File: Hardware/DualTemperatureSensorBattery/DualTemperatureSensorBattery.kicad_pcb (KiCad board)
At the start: 2 copper layers, 67.5 x 24.2 mm, 22 parts, among them J2 Conn_01x06, Q101 BSS84, SW2 SW_Push, U1 ME54BS01_V1.0

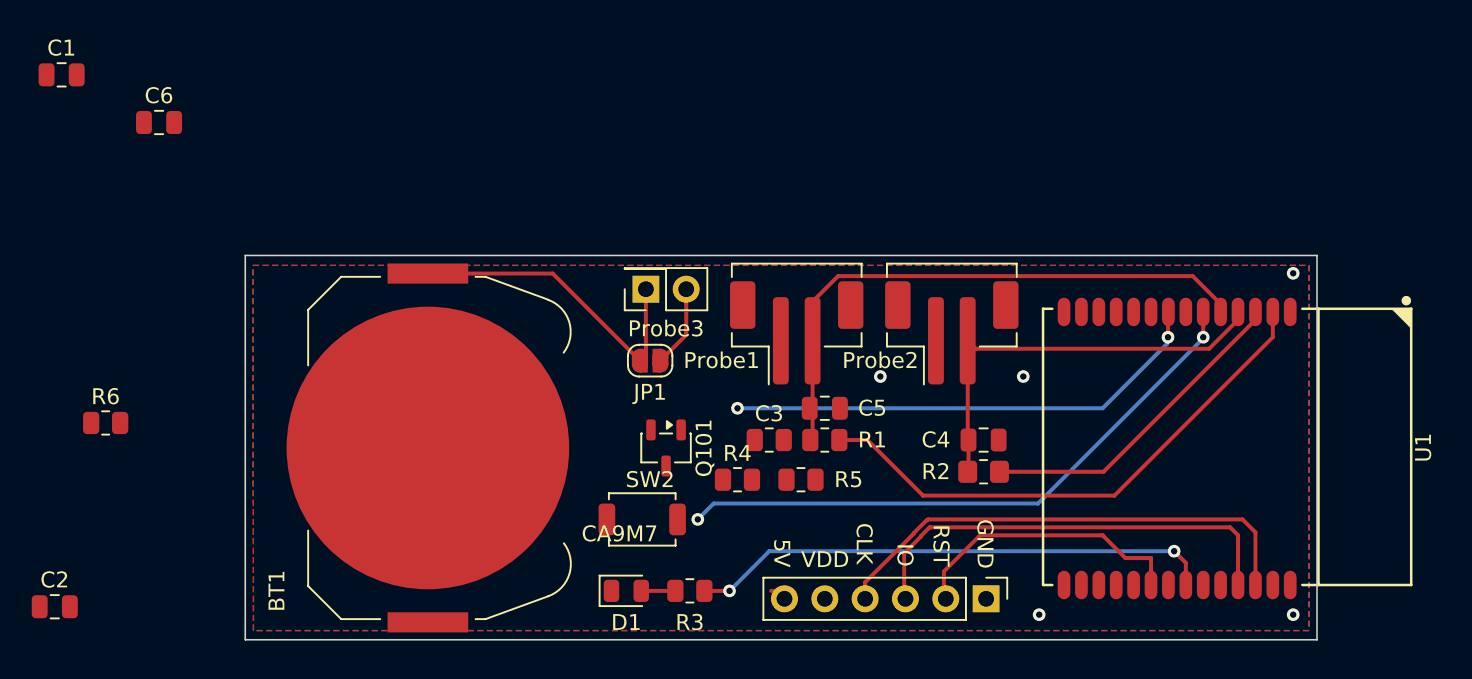
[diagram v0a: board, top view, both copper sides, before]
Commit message: Rename the project. Finish routing.
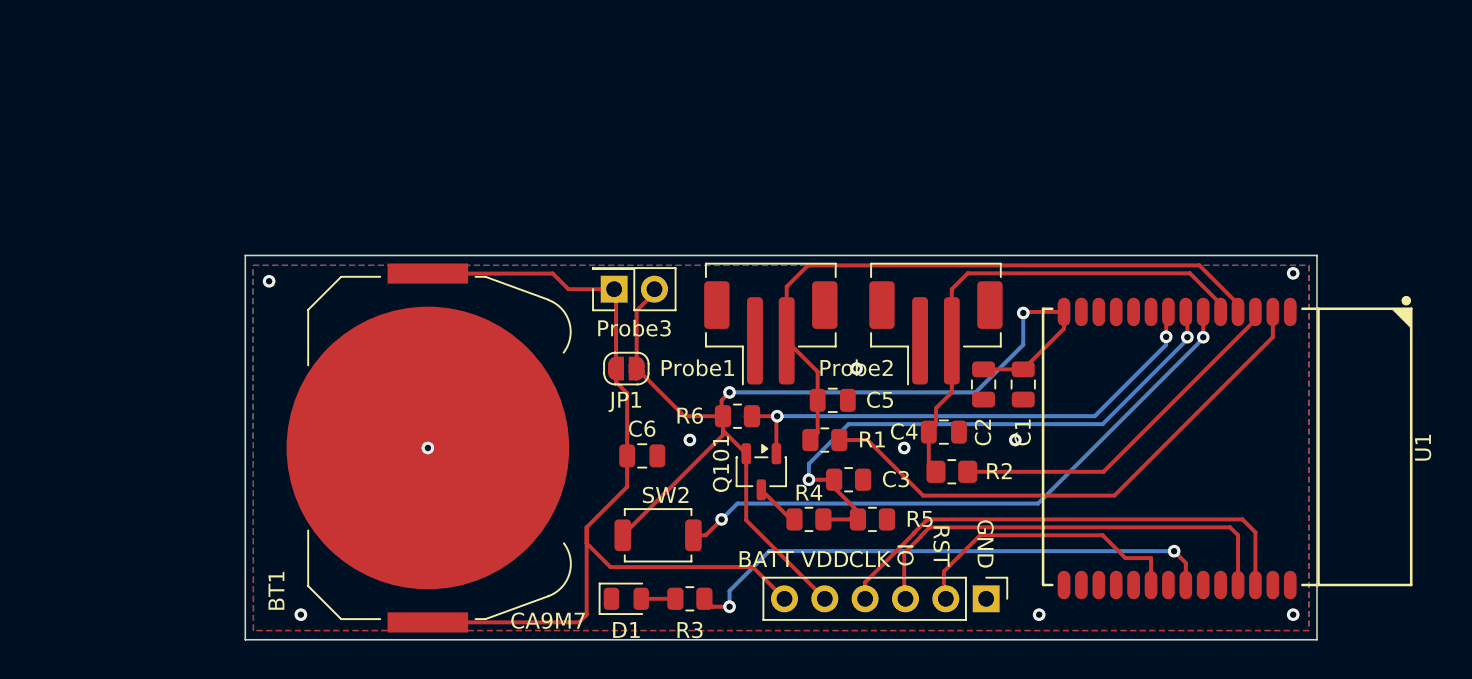
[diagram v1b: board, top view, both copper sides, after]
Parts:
- moved C1 63.6 mm to (76.0, 63.5), turned to -90 degrees
- moved C2 60.2 mm to (73.5, 63.5), turned to -90 degrees
- moved R6 39.8 mm to (58.0, 65.5)
- moved C6 37.0 mm to (52.0, 68.0)
- moved Q101 6.18 mm to (59.5, 69.0)
- moved C3 5.59 mm to (65.0, 69.5)
- moved R4 5.15 mm to (62.5, 72.0)
- moved R5 5.15 mm to (66.5, 72.0)
- moved C4 2.55 mm to (71.0, 66.5)
- moved Probe3 2.00 mm to (50.2, 57.5)
- moved R2 2.00 mm to (71.5, 69.0)
- moved Probe1 1.63 mm to (60.1, 60.2)
- moved JP1 1.58 mm to (51.0, 62.5)
- moved SW2 1.41 mm to (53.0, 73.0)
- moved Probe2 1.00 mm to (70.5, 60.2)
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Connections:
- BT1 pad 1: Net-(BT1-+) -> +BATT
- C6 pad 1: Net-(BT1-+) -> +BATT
- J2 pad 6: VDD -> +BATT
- JP1 pad 1: Net-(BT1-+) -> +BATT
- Probe3 pad 1: Net-(BT1-+) -> +BATT
- U1 pad 4: PROBE_2_DIVIDER -> PROBE_1_DIVIDER
- U1 pad 5: PROBE_1_DIVIDER -> PROBE_2_DIVIDER
- U1 pad 7: Enable-Battery -> V_{BAT}
- U1 pad 8: V_{BAT} -> Enable-Battery
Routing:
- net VDD: track 6.22 -> 70.0 mm, vias 0 -> 2
- net +BATT: track 0.00 -> 59.4 mm
- net Enable-Battery: track 0.00 -> 33.0 mm, vias 0 -> 2
- net Net-(BT1-+): track 20.3 -> 0.00 mm
- net PROBE_1_DIVIDER: track 37.5 -> 43.5 mm
- net V_{BAT}: track 30.9 -> 36.4 mm
- net PROBE_2_DIVIDER: track 26.8 -> 30.9 mm
- net Net-(Q101-D): track 0.00 -> 2.86 mm
- net PROBE_2_PWR: track 20.6 -> 22.7 mm
- net GND: track 1.82 -> 0.00 mm, vias 5 -> 10
- net LED: track 33.3 -> 34.8 mm
- net BUTTON: track 38.2 -> 38.9 mm
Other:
- board text added: "BATT"
- board text removed: "5V"

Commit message: Removed the battery measurement. Reworked some of the layout.
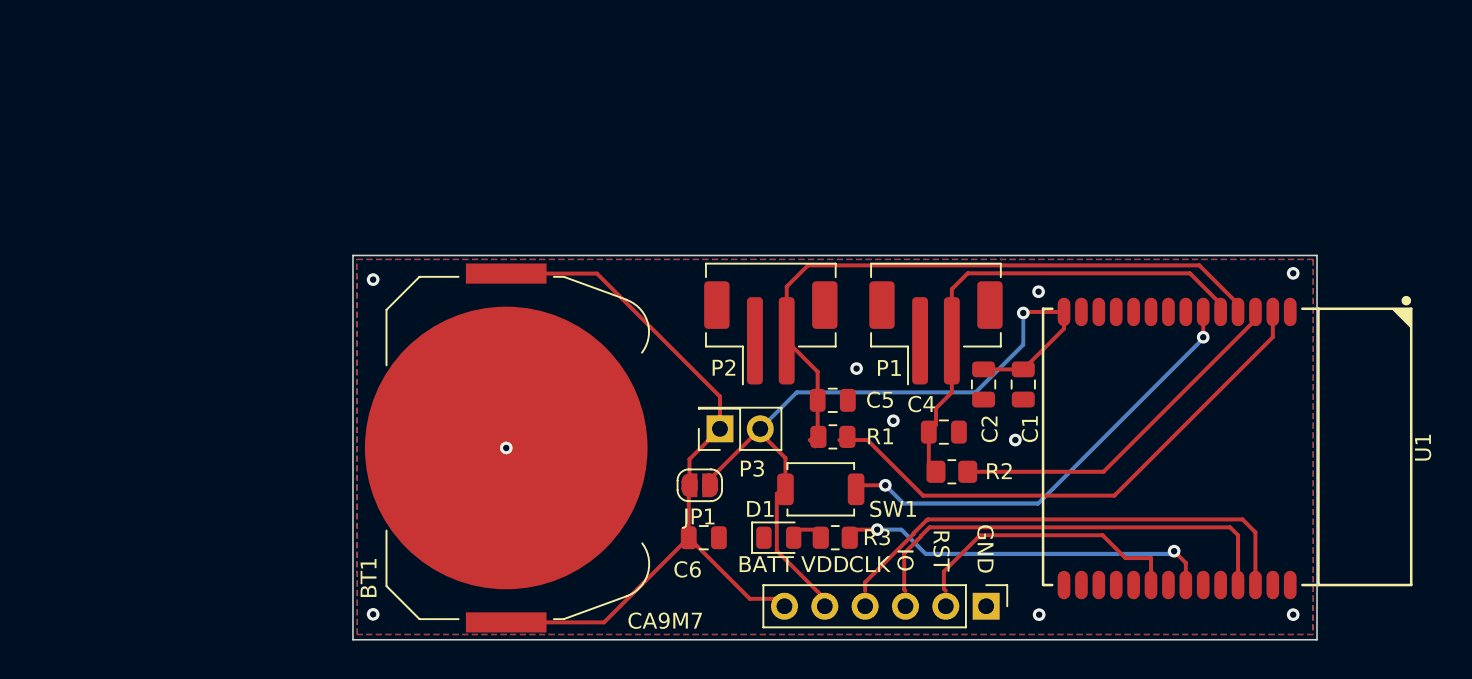
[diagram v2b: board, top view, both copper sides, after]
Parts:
- removed C3: 1n, Resistor_SMD:R_0805_2012Metric
- removed Q101: BSS84, Package_TO_SOT_SMD:SOT-23-3
- removed R4: 8k2, Resistor_SMD:R_0805_2012Metric
- removed R5: 2k2, Resistor_SMD:R_0805_2012Metric
- removed R6: 1M, Resistor_SMD:R_0805_2012Metric
- R3: value 220 -> 330
- moved P3 11.0 mm to (56.9, 66.3)
- moved SW1 10.6 mm to (63.2, 70.1)
- moved D1 10.3 mm to (60.6, 73.2)
- moved R3 9.93 mm to (64.2, 73.2)
- moved JP1 8.68 mm to (55.6, 69.8)
- moved C6 6.45 mm to (55.9, 73.2)
- moved BT1 4.93 mm to (43.4, 67.5)
- moved R1 0.55 mm to (64.0, 66.8)
- moved J2 0.47 mm to (73.7, 77.5)
- renumbered Probe2 to P1, Probe1 to P2, Probe3 to P3, SW2 to SW1
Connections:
- U1 pad 7: V_{BAT} -> unconnected-(U1-P1.14/AIN7-Pad7)
- U1 pad 8: Enable-Battery -> unconnected-(U1-P1.06/AIN2-Pad8)
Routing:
- net V_{BAT}: track 36.4 -> 0.00 mm, vias 2 -> 0
- net Enable-Battery: track 33.0 -> 0.00 mm, vias 2 -> 0
- net VDD: track 70.0 -> 48.3 mm, vias 2 -> 1
- net +BATT: track 59.4 -> 47.7 mm
- net LED: track 34.8 -> 23.6 mm
- net BUTTON: track 38.9 -> 28.3 mm
- net Net-(Q101-D): track 2.86 -> 0.00 mm
- net GND: track 0.00 -> 1.00 mm
- net unconnected-(U1-P1.06/AIN2-Pad8): track 0.00 -> 0.53 mm
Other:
- board size 67.5 x 24.2 mm -> 60.7 x 24.2 mm
- board text added: "@tomasmcguinness Dual Temperature Sensor REVISION ${REVISION}"
- board text added: "P2"
- board text removed: "@tomasmcguinness Dual Temperature Sensor nRF54L15 REVISION ${REVISION}"
